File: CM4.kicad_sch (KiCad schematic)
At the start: 0 parts

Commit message: minor changes/cleanup
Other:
- removed sheet LanCM4
- removed sheet PinoutCM4
- added sheet CM4_Module1A (CM4_Module1A.kicad_sch)
- added sheet CM4_Module1B (CM4_Module1B.kicad_sch)

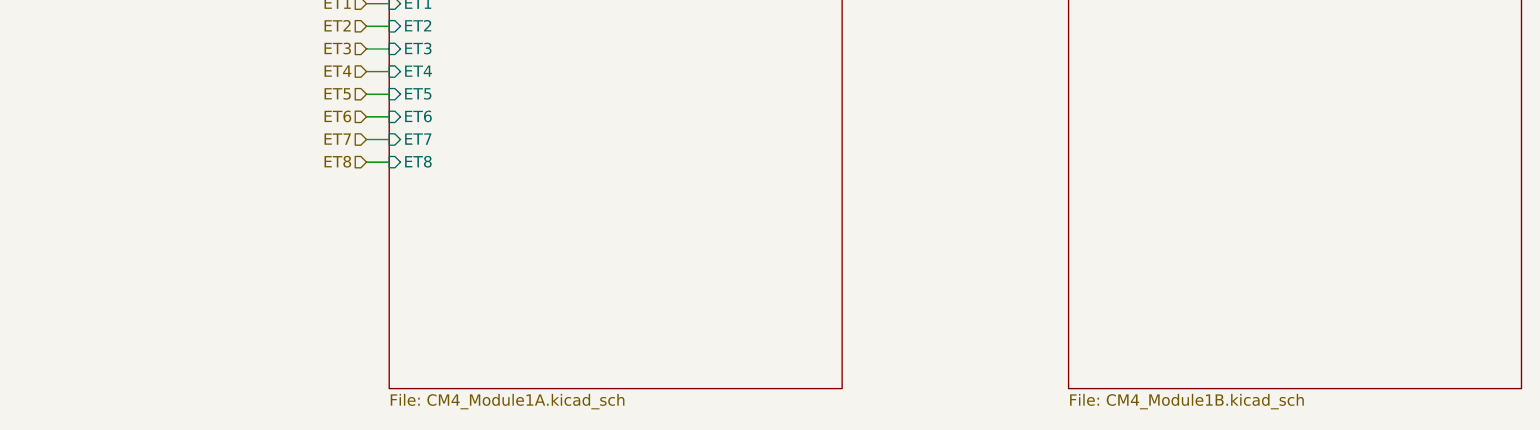
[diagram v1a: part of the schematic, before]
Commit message: WIFI connection changes PI
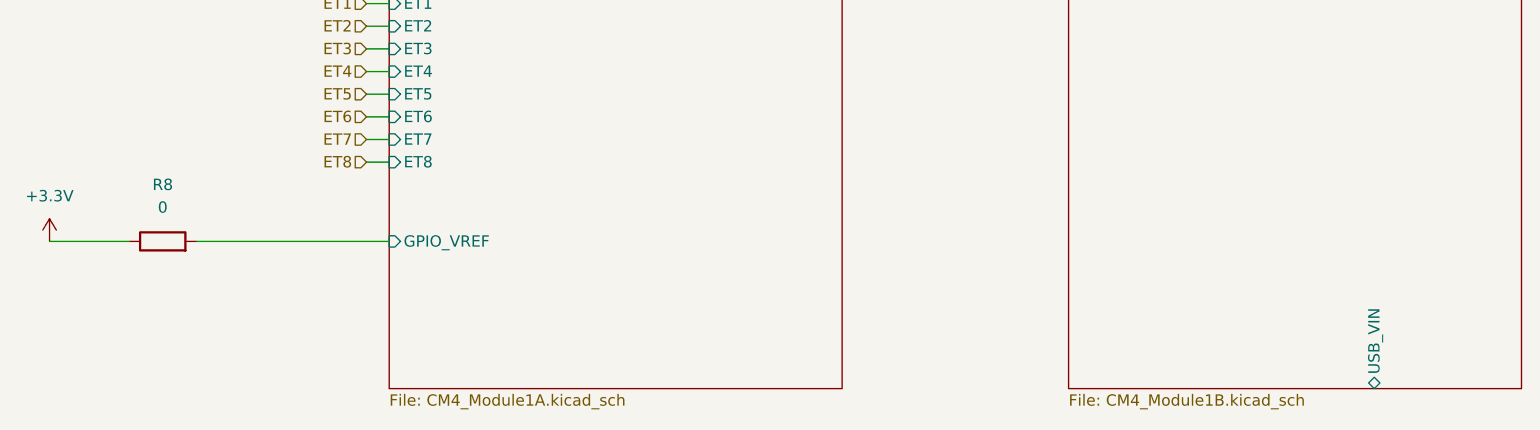
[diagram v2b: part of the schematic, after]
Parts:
- added R8: 0, Resistor_SMD:R_0603_1608Metric, symbol #dzdb:g_res/R-0-0603
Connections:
- new net +3.3V: R8.1
- new net CM4_Module1A/GPIO_VREF: R8.2
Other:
- sheet CM4_Module1A ports: added GPIO_VREF; removed none
- sheet CM4_Module1B ports: added USB_VIN; removed none

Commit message: nothing
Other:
- sheet CM4_Module1A ports: added RXD0, TXD0; removed none
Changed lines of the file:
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@@
+	(wire
+		(pts
+			(xy 124.46 97.79) (xy 124.46 104.14)
+		)
+		(stroke
+			(width 0)
+			(type default)
+		)
+	)
 	(wire
 		(pts
@@
 	(wire
 		(pts
+			(xy 128.27 97.79) (xy 128.27 104.14)
+		)
+		(stroke
+			(width 0)
+			(type default)
+		)
+	)
+	(wire
+		(pts
 			(xy 83.82 72.39) (xy 86.36 72.39)
 		)
@@
 		)
 	)
+	(hierarchical_label "PI_RX"
+		(shape input)
+		(at 128.27 104.14 270)
+		(effects
+			(font
+				(size 1.27 1.27)
+			)
+			(justify right)
+		)
+	)
 	(hierarchical_label "ET1"
 		(shape input)
@@
 		(shape input)
 		(at 83.82 72.39 180)
+		(effects
+			(font
+				(size 1.27 1.27)
+			)
+			(justify right)
+		)
+	)
+	(hierarchical_label "PI_TX"
+		(shape input)
+		(at 124.46 104.14 270)
 		(effects
 			(font
@@
 			(effects
 				(font
+					(size 1.27 1.27)
+				)
+				(justify left)
+			)
+		)
+		(pin "RXD0" input
+			(at 128.27 97.79 270)
+			(effects
+				(font
+					(size 1.27 1.27)
+				)
+				(justify left)
+			)
+		)
+		(pin "TXD0" input
+			(at 124.46 97.79 270)
+			(effects
+				(font

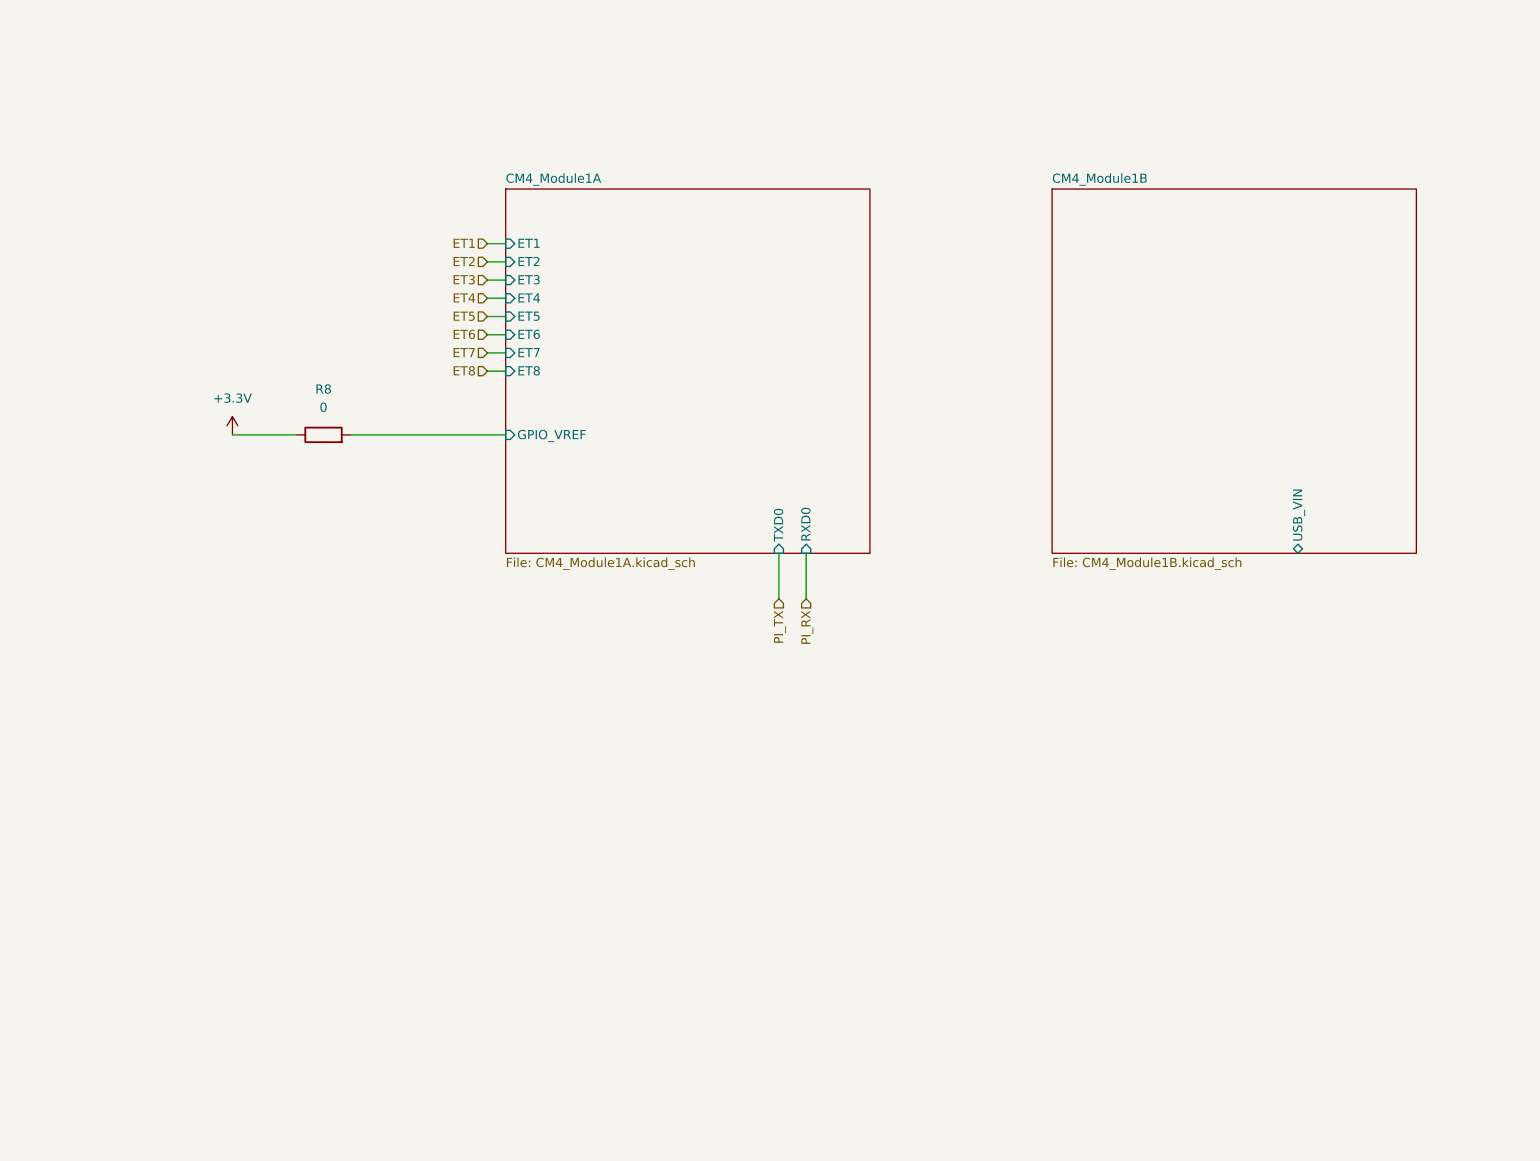
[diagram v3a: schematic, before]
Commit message: added more support for the ssd and fixed LED configuration
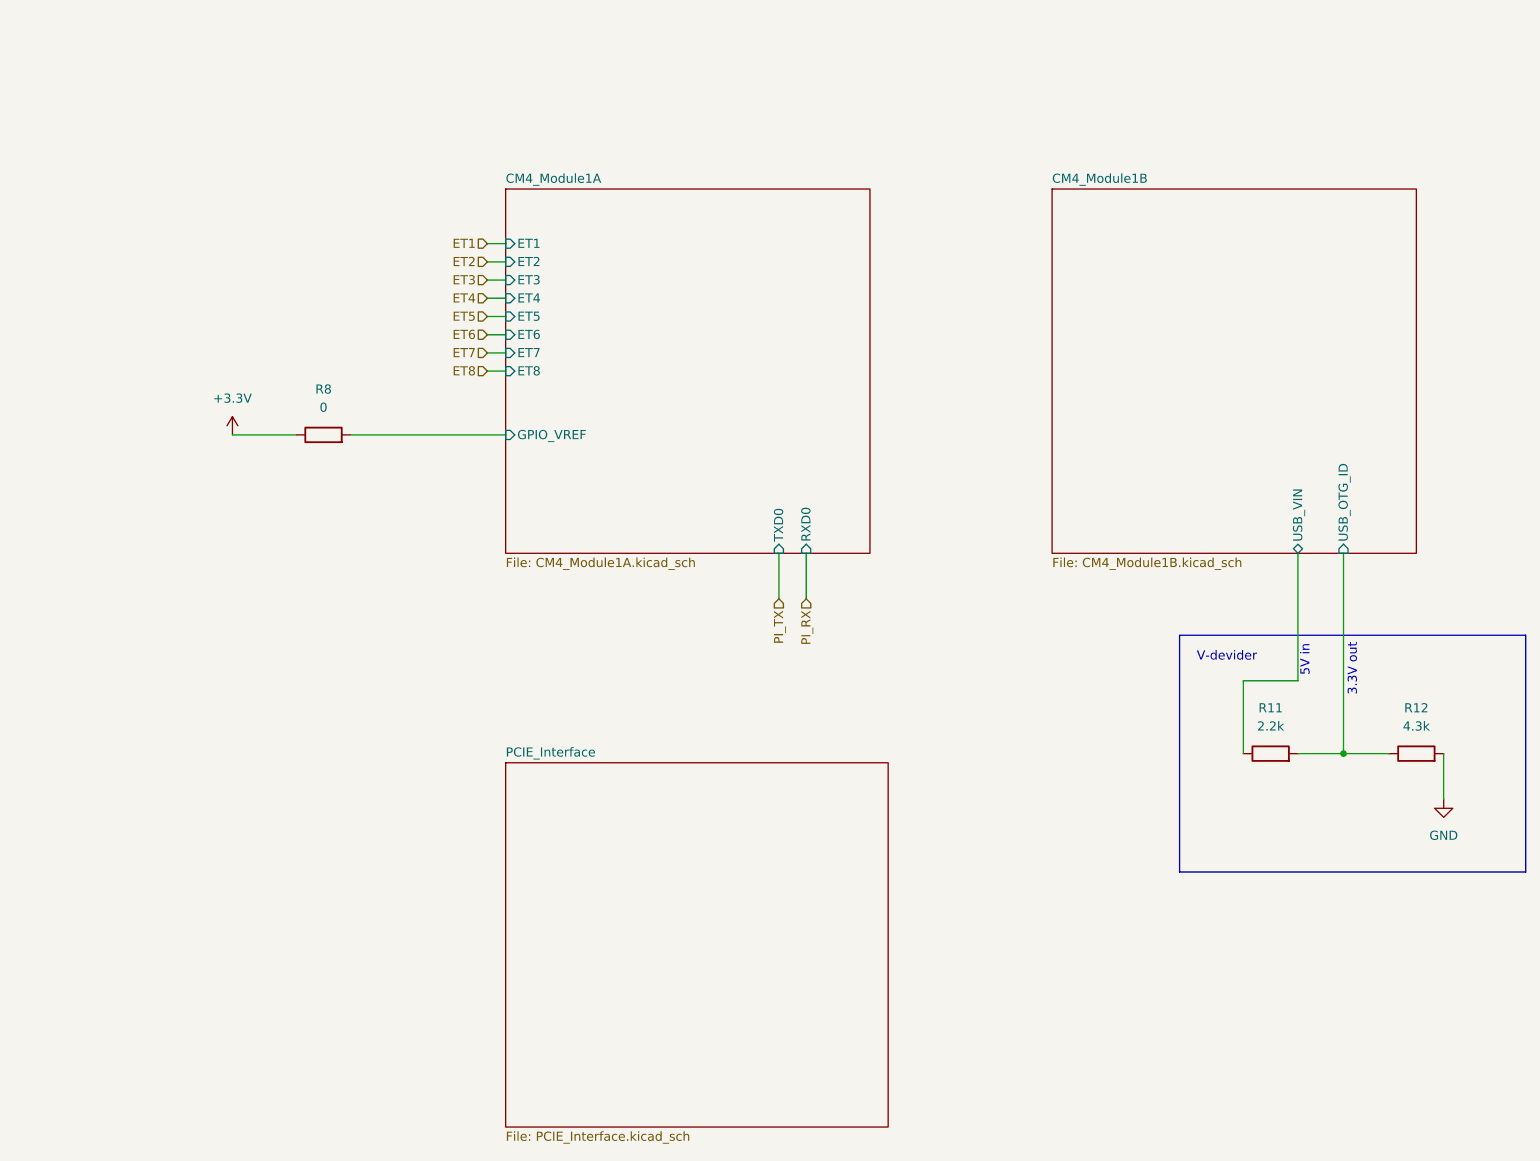
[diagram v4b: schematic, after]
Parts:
- added R11: 2.2k, Resistor_SMD:R_0603_1608Metric, symbol #dzdb:g_res/R-2.2k-0603
- added R12: 4.3k, Resistor_SMD:R_0603_1608Metric, symbol #dzdb:g_res/R-4.3k-0603
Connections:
- net CM4_Module1B/USB_VIN: now also R11.1
- new net CM4_Module1B/USB_OTG_ID: R11.2, R12.1
- new net GND: R12.2
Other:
- added sheet PCIE_Interface (PCIE_Interface.kicad_sch)
- sheet CM4_Module1B ports: added USB_OTG_ID; removed none
- note added: "3.3V out"
- note added: "5V in"
- note added: "V-devider"

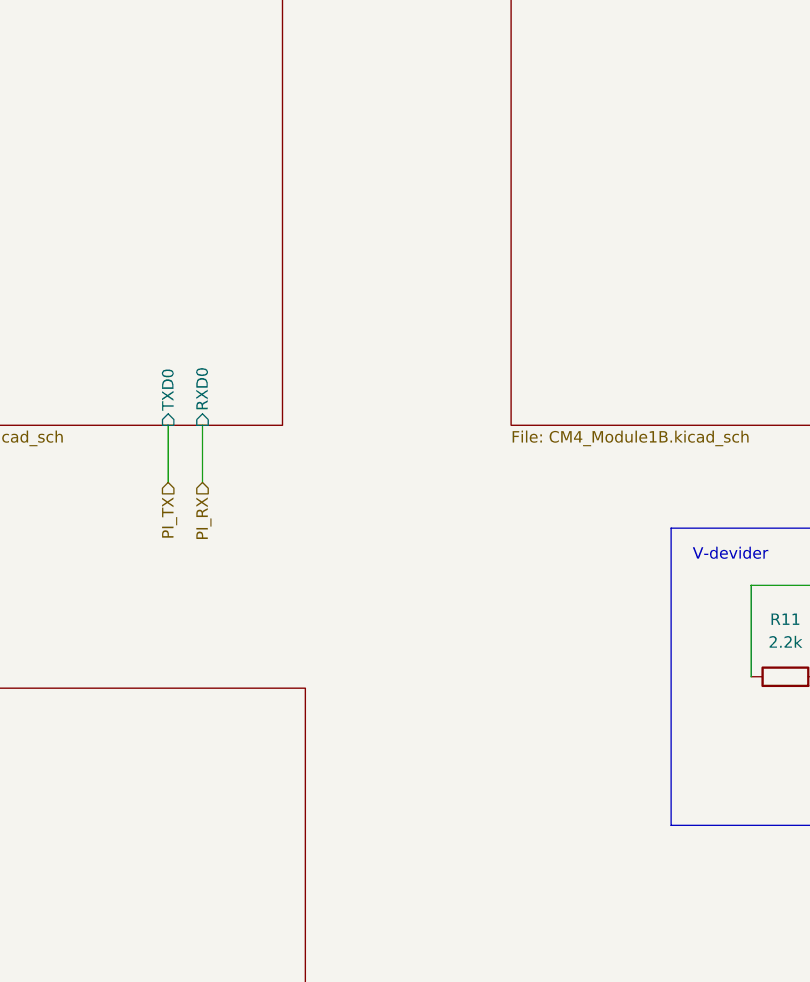
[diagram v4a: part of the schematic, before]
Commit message: multiple changes. fixed some mistakes, added jumper pins for wifi
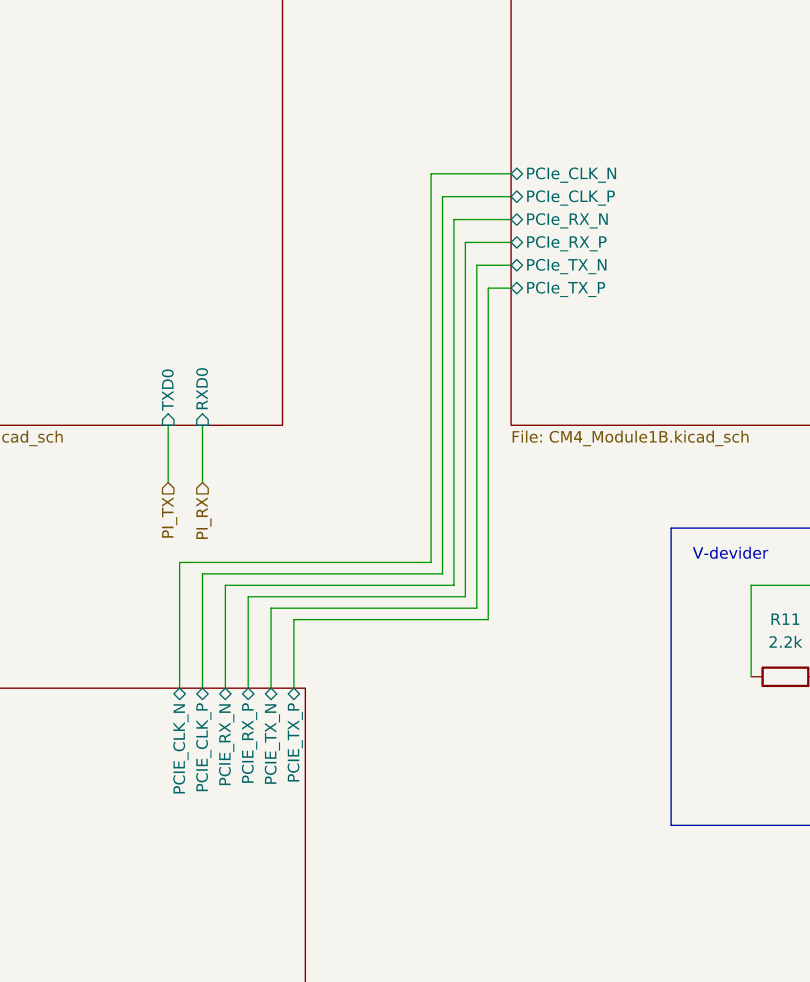
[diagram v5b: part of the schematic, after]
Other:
- sheet CM4_Module1B ports: added PCIe_CLK_N, PCIe_CLK_P, PCIe_RX_N, PCIe_RX_P, PCIe_TX_N, PCIe_TX_P; removed none
- sheet PCIE_Interface ports: added PCIE_CLK_N, PCIE_CLK_P, PCIE_RX_N, PCIE_RX_P, PCIE_TX_N, PCIE_TX_P; removed none

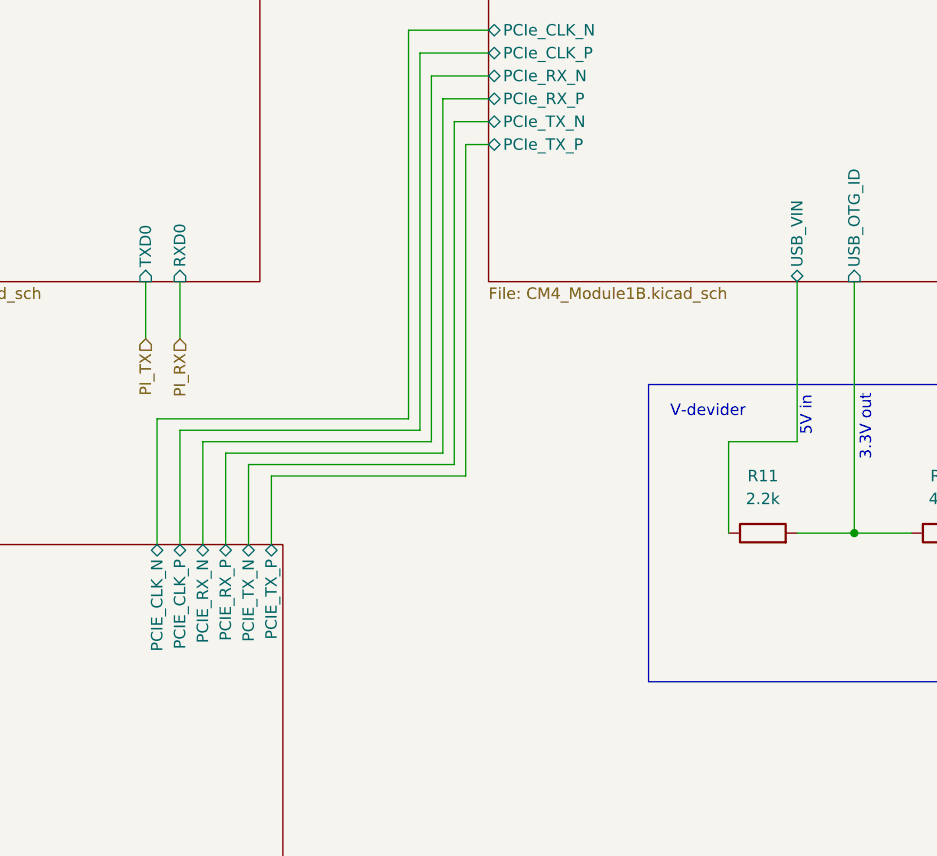
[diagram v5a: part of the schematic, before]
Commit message: added comment boxes
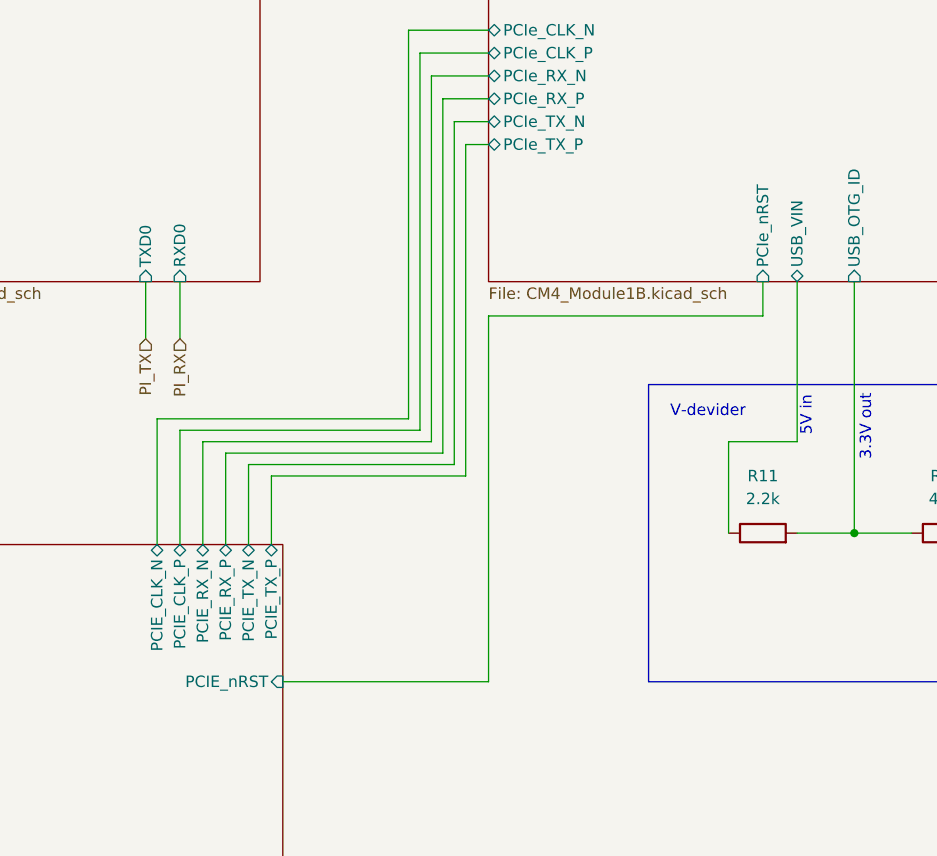
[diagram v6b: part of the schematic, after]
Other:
- sheet CM4_Module1B ports: added PCIe_nRST; removed none
- sheet PCIE_Interface ports: added PCIE_nRST; removed none
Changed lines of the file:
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@@
+	(wire
+		(pts
+			(xy 193.04 101.6) (xy 193.04 97.79)
+		)
+		(stroke
+			(width 0)
+			(type default)
+		)
+	)
 	(wire
 		(pts
@@
 	(wire
 		(pts
+			(xy 162.56 142.24) (xy 162.56 101.6)
+		)
+		(stroke
+			(width 0)
+			(type default)
+		)
+	)
+	(wire
+		(pts
 			(xy 160.02 82.55) (xy 162.56 82.55)
 		)
@@
 	(wire
 		(pts
+			(xy 162.56 101.6) (xy 193.04 101.6)
+		)
+		(stroke
+			(width 0)
+			(type default)
+		)
+	)
+	(wire
+		(pts
 			(xy 130.81 115.57) (xy 130.81 127)
 		)
@@
 		(pts
 			(xy 203.2 125.73) (xy 209.55 125.73)
+		)
+		(stroke
+			(width 0)
+			(type default)
+		)
+	)
+	(wire
+		(pts
+			(xy 139.7 142.24) (xy 162.56 142.24)
 		)
 		(stroke
@@
 			)
 		)
+		(pin "PCIe_nRST" input
+			(at 193.04 97.79 270)
+			(effects
+				(font
+					(size 1.27 1.27)
+				)
+				(justify left)
+			)
+		)
 		(instances
 			(project "nautilus_mainboard"
@@
 			(effects
 				(font
+					(size 1.27 1.27)
+				)
+				(justify right)
+			)
+		)
+		(pin "PCIE_nRST" input
+			(at 139.7 142.24 0)
+			(effects
+				(font

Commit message: Added Power logic finally. (plus some comments on further improvements)
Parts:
- removed R8: 0, Resistor_SMD:R_0603_1608Metric, symbol #dzdb:g_res/R-0-0603
- renumbered R11 to R1, R12 to R2
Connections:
- net CM4_Module1B/USB_VIN renamed CM4_Module1B/USB_OTG_5V
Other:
- sheet CM4_Module1B ports: added USB_OTG_5V; removed USB_VIN
